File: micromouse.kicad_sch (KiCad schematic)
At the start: 17 parts, among them U1 STM32L4R9AIIx, U2 DRV8231DSGR

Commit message: Test file
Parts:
- removed U2: DRV8231DSGR, Package_SON:WSON-8-1EP_2x2mm_P0.5mm_EP0.9x1.6mm, symbol DRV8321:DRV8231DSGR
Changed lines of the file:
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@@
     (pin "2")
-  )
-  (symbol (lib_id "DRV8321:DRV8231DSGR") (at 455.93 110.49 0) (unit 1)
-    (in_bom yes) (on_board yes) (fields_autoplaced)
-    (property "Reference" "U2" (id 0) (at 476.25 99.06 0)
-      (effects (font (size 1.524 1.524)))
-    )
-    (property "Value" "DRV8231DSGR" (id 1) (at 476.25 102.87 0)
-      (effects (font (size 1.524 1.524)))
-    )
-    (property "Footprint" "Package_SON:WSON-8-1EP_2x2mm_P0.5mm_EP0.9x1.6mm" (id 2) (at 476.25 104.394 0)
-      (effects (font (size 1.524 1.524)) hide)
-    )
-    (property "Datasheet" "" (id 3) (at 455.93 110.49 0)
-      (effects (font (size 1.524 1.524)))
-    )
-    (pin "1")
-    (pin "2")
-    (pin "3")
-    (pin "4")
-    (pin "5")
-    (pin "6")
-    (pin "7")
-    (pin "8")
-    (pin "9")
   )
   (symbol (lib_id "Device:C") (at 110.49 25.4 180) (unit 1)
@@
       (reference "U1") (unit 1) (value "STM32L4R9AIIx") (footprint "Package_BGA:UFBGA-169_7x7mm_Layout13x13_P0.5mm")
     )
-    (path "/4e296cff-f0ff-4f2a-83f3-fd28d526450d"
-      (reference "U2") (unit 1) (value "DRV8231DSGR") (footprint "Package_SON:WSON-8-1EP_2x2mm_P0.5mm_EP0.9x1.6mm")
-    )
-  )
+    (path "/fcad3790-4569-48af-b3e3-af34c79fc3e5/08c0cc85-505b-4fa7-9048-439db4c7496d"
+      (reference "U?") (unit 1) (value "DRV8231DSGR") (footprint "Package_SON:WSON-8-1EP_2x2mm_P0.5mm_EP0.9x1.6mm")
+    )
+  )

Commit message: merge files for presentation
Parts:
- added C? (x5): 4,7u, symbol Device:C
- added C? (x4): 1 uF, symbol pspice:C
- added C? (x2): 100u, symbol Device:C_Polarized_US
- added C? (x8): 100n, symbol Device:C
- added C? (x5): 0.1u, symbol Device:C
- added C?: 4,7µF, symbol Device:C
- added C?: 30µF, symbol Device:C
- added C?: 0,1µF, symbol Device:C
- added IC?: 5v to 3.3v, TPS7A0333PYCHR:BGA4C35P2X2_64X64X40, symbol TPS7A0333PYCHR:TPS7A0333PYCHR
- added J?: connecteur batterie, symbol Connector_Generic:Conn_01x02
- added J? (x2): IDC MALE, symbol Connector_Generic:Conn_02x03_Odd_Even
- added L?: 2.2µH, symbol Device:L
- added LED? (x5): SFH_4550, SFH4550, symbol SFH_4550:SFH_4550
- added Q? (x5): Q_NMOS_DGS, symbol Device:Q_NMOS_DGS
- added Q? (x4): TEFT4300, TEFT4300, symbol TEFT4300:TEFT4300
- added R? (x5): 0.56, symbol Device:R
- added R? (x2): 50k, symbol Device:R
- added R? (x7): 10k, symbol Device:R
- added R? (x4): 1k8, symbol Device:R
- added R? (x2): 1k, symbol Device:R
- added R?: 50kΩ, symbol Device:R
- added R?: 10kΩ, symbol Device:R
- added S?: Switch, ESE-20C343:ESE20C343, symbol ESE-20C343:ESE-20C343
- added U?: MAX20077ATCA/VY+, symbol MAX20077ATCA-VY:MAX20077ATCA/VY+
- added U?: 3.3v to 1.8v, symbol TPS7A0318PYCHR:TPS7A0318PYCHR
- added U? (x2): DRV8231DSGR, Package_SON:WSON-8-1EP_2x2mm_P0.5mm_EP0.9x1.6mm, symbol DRV8321:DRV8231DSGR
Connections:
- net GND: now also C?.1, C?.1, C?.2, C?.2, C?.2, C?.2, C?.2, C?.2, C?.2, C?.2, C?.2, C?.2, C?.2, C?.2, C?.2, C?.2, C?.2, C?.2, C?.2, C?.2, C?.2, C?.2, C?.2, C?.2, C?.2, C?.2, IC?.B2 (GND), J?.4 (Pin_4), J?.4 (Pin_4), Q?.3 (S), Q?.3 (S), Q?.3 (S), Q?.3 (S), Q?.3 (S), R?.1, R?.1, R?.1, R?.1, R?.1, R?.2, R?.2, R?.2, R?.2, R?.2, R?.2, R?.2, R?.2, R?.2, S?.B1 (NO_1), U?.1 (GND), U?.1 (GND), U?.13 (EPAD), U?.6 (PGND), U?.7 (AGND), U?.B2 (GND)
- new net: Q?.1 (D), R?.2 (x5)
- new net: LED?.1, R?.1 (x5)
- new net: J?.3 (Pin_3), R?.1, R?.1 (x2)
- new net: J?.2 (Pin_2), S?.A1 (COM_1)
- new net: U?.10 (BIAS), U?.11 (SYNC), U?.12 (PGOOD)
- new net: C?.2, U?.3 (BST)
- new net: C?.1, L?.1, U?.5 (LX)
- new net: R?.1, R?.2, U?.8 (FB)
- new net +1V8: C?.1, C?.1, C?.1, C?.1, C?.1, C?.1, C?.1, C?.1, C?.1, C?.1, C?.1, LED?.2, LED?.2, LED?.2, LED?.2, LED?.2, U?.A2 (OUT)
- new net +3.3V: C?.1, C?.1, C?.1, C?.1, C?.1, C?.1, IC?.A2 (OUT), Q?.2 (C), Q?.2 (C), Q?.2 (C), Q?.2 (C), U?.4 (VREF), U?.4 (VREF), U?.A1 (IN), U?.B1 (EN)
- new net +6V: C?.1, C?.1, C?.1, C?.1, C?.1, C?.1, IC?.A1 (IN), IC?.B1 (EN), L?.2, R?.1, R?.2, R?.2, U?.5 (VM), U?.5 (VM), U?.9 (OUT)
- new net +BATT: C?.1, J?.1 (Pin_1), U?.2 (EN), U?.4 (SUP)
- new net IR_PILOT: Q?.2 (G), Q?.2 (G), Q?.2 (G), Q?.2 (G), Q?.2 (G), R?.2, R?.2, R?.2, R?.2, R?.2
- new net MOTOR1+: J?.1 (Pin_1), U?.8 (OUT2)
- new net MOTOR1-: J?.2 (Pin_2), U?.6 (OUT1)
- new net MOTOR1_A: J?.6 (Pin_6)
- new net MOTOR1_B: J?.5 (Pin_5)
- new net MOTOR1_IN1: U?.3 (IN1)
- new net MOTOR1_IN2: U?.2 (IN2)
- new net MOTOR1_ISENSE: C?.2, C?.2, R?.1, R?.1, U?.7 (ISEN), U?.7 (ISEN)
- new net MOTOR2+: J?.1 (Pin_1), U?.8 (OUT2)
- new net MOTOR2-: J?.2 (Pin_2), U?.6 (OUT1)
- new net MOTOR2_A: J?.6 (Pin_6)
- new net MOTOR2_B: J?.5 (Pin_5)
- new net MOTOR2_IN1: U?.3 (IN1)
- new net MOTOR2_IN2: U?.2 (IN2)
- new net PHOTO_L: Q?.1 (E), R?.1
- new net PHOTO_LS: Q?.1 (E), R?.1
- new net PHOTO_R: Q?.1 (E), R?.1
- new net PHOTO_RS: Q?.1 (E), R?.1
- no-connect marks 0 -> 5
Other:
- removed sheet Alimentations
- removed sheet Motors drivers
- note added: "Encodeurs IEH2"
- note added: "Hacheur 4.5v-33v - 3.7A"
- note added: "IR Receiver"
- note added: "IR Transmitters"
- moved on the sheet: C1, C10, C11, C12, C13, C14, C15, C2, C3, C4, C5, C6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

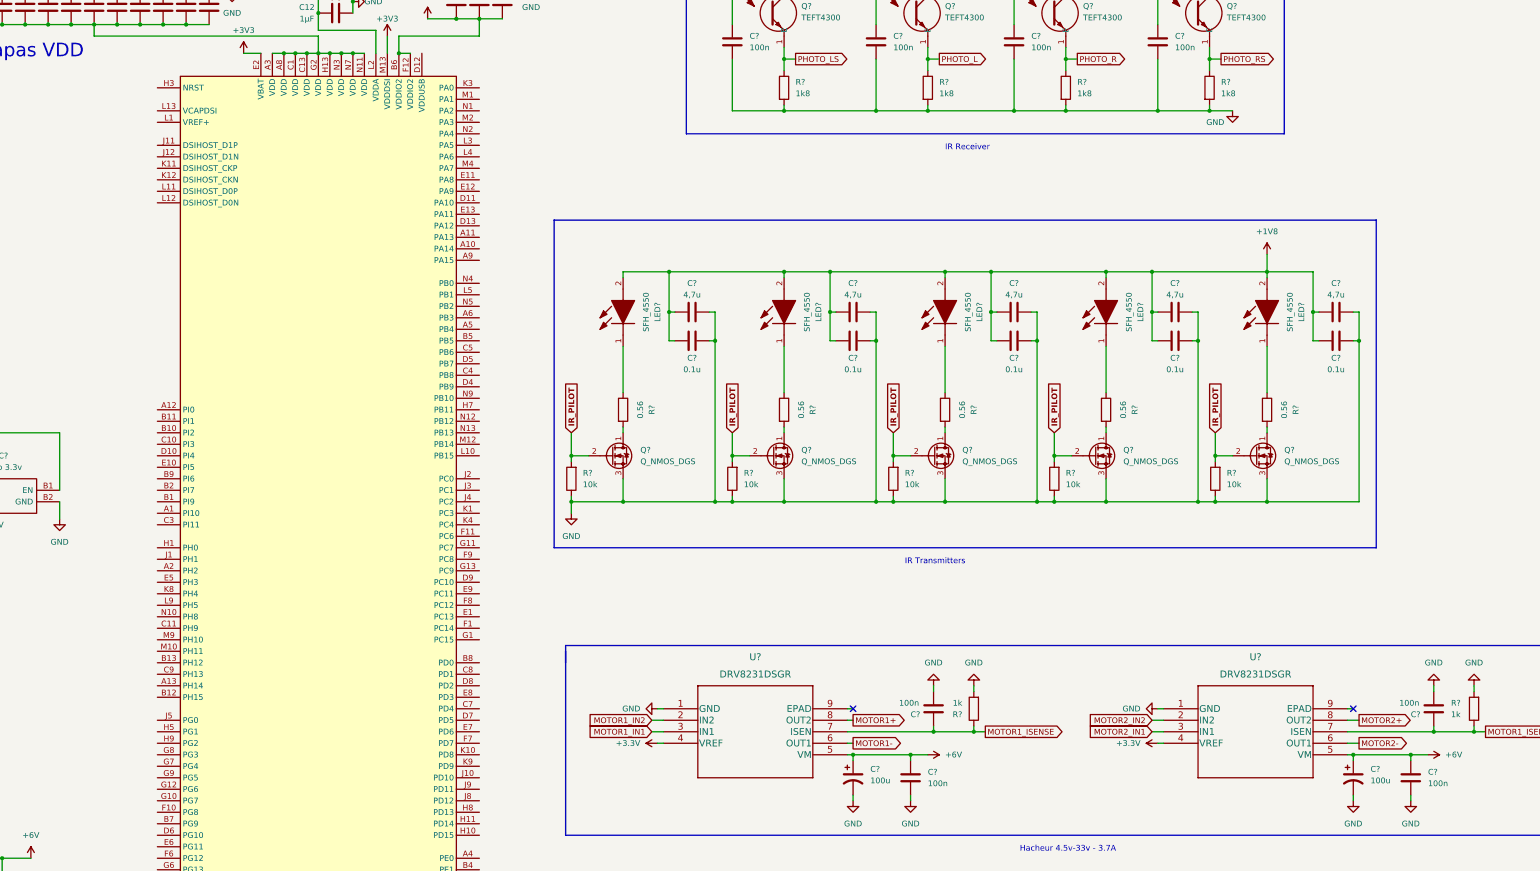
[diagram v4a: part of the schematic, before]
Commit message: added pin on mcu
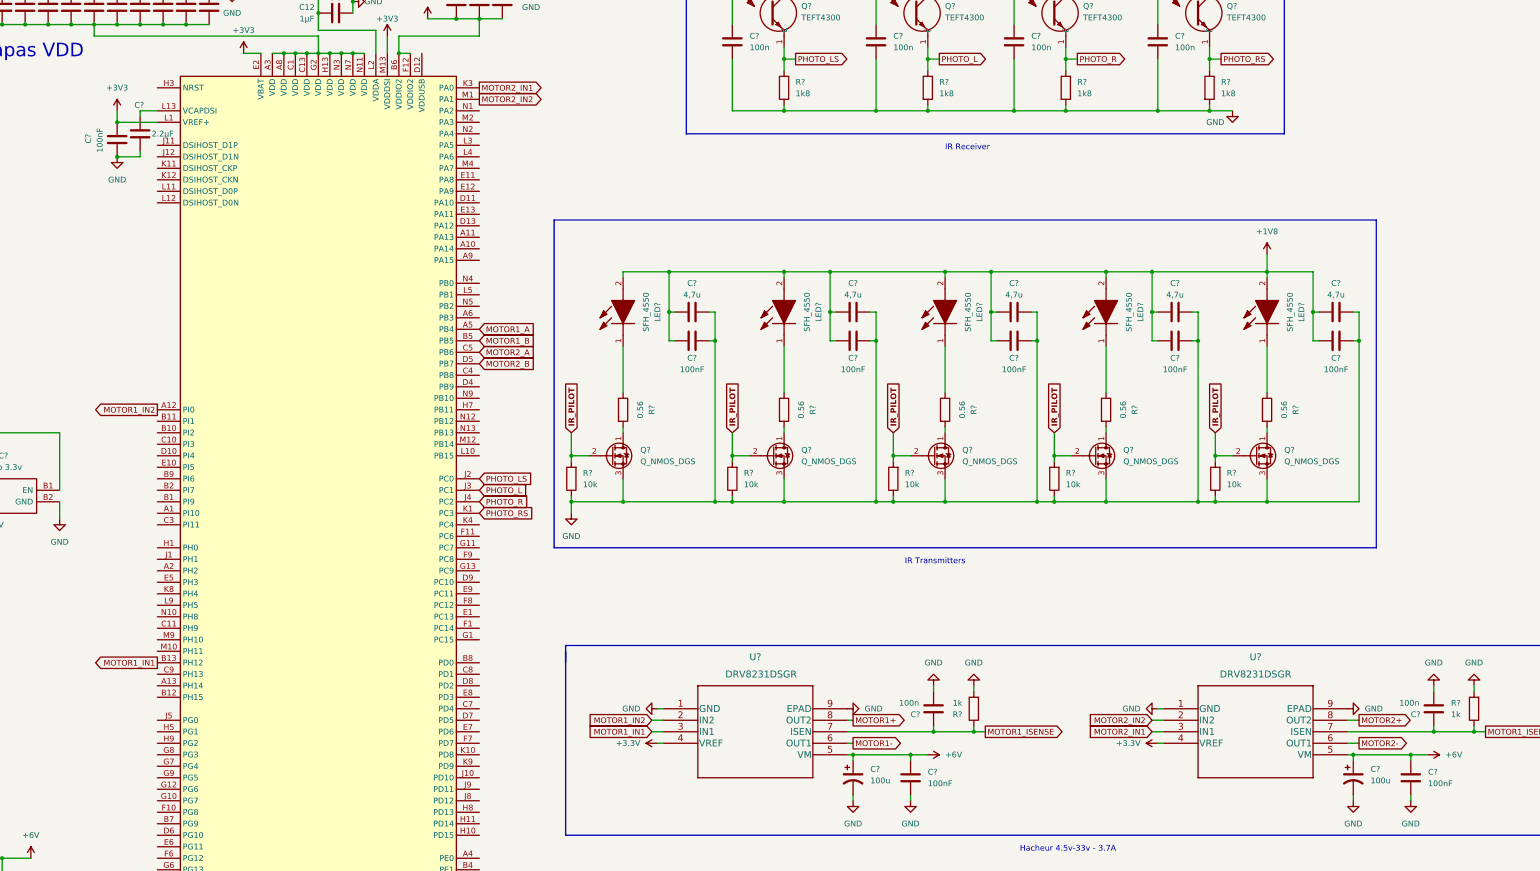
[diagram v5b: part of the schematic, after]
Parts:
- added C?: 100nF, symbol Device:C
- added C?: 2.2µF, symbol Device:C
- C? (x5): value 0.1u -> 100nF
- C? (x2): value 100n -> 100nF
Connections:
- net +3V3: now also U1.L1 (VREF+), C?.2
- net GND: now also U?.9 (EPAD), U?.9 (EPAD), C?.1, C?.2
- net MOTOR1_A: now also U1.A5 (PB4)
- net MOTOR1_B: now also U1.B5 (PB5)
- net MOTOR1_IN1: now also U1.B13 (PH12)
- net MOTOR1_IN2: now also U1.A12 (PI0)
- net MOTOR2_A: now also U1.C5 (PB6)
- net MOTOR2_B: now also U1.D5 (PB7)
- net MOTOR2_IN1: now also U1.K3 (PA0)
- net MOTOR2_IN2: now also U1.M1 (PA1)
- net PHOTO_L: now also U1.J3 (PC1)
- net PHOTO_LS: now also U1.J2 (PC0)
- net PHOTO_R: now also U1.J4 (PC2)
- net PHOTO_RS: now also U1.K1 (PC3)
- net at U1.L13 (VCAPDSI): now also C?.1
- no-connect marks 5 -> 3
